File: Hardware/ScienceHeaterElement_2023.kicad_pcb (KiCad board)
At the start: 2 copper layers, 127 x 127.1 mm, 10 parts, among them Q1 BUK7M6R3-40EX, U1 LMT85DCK

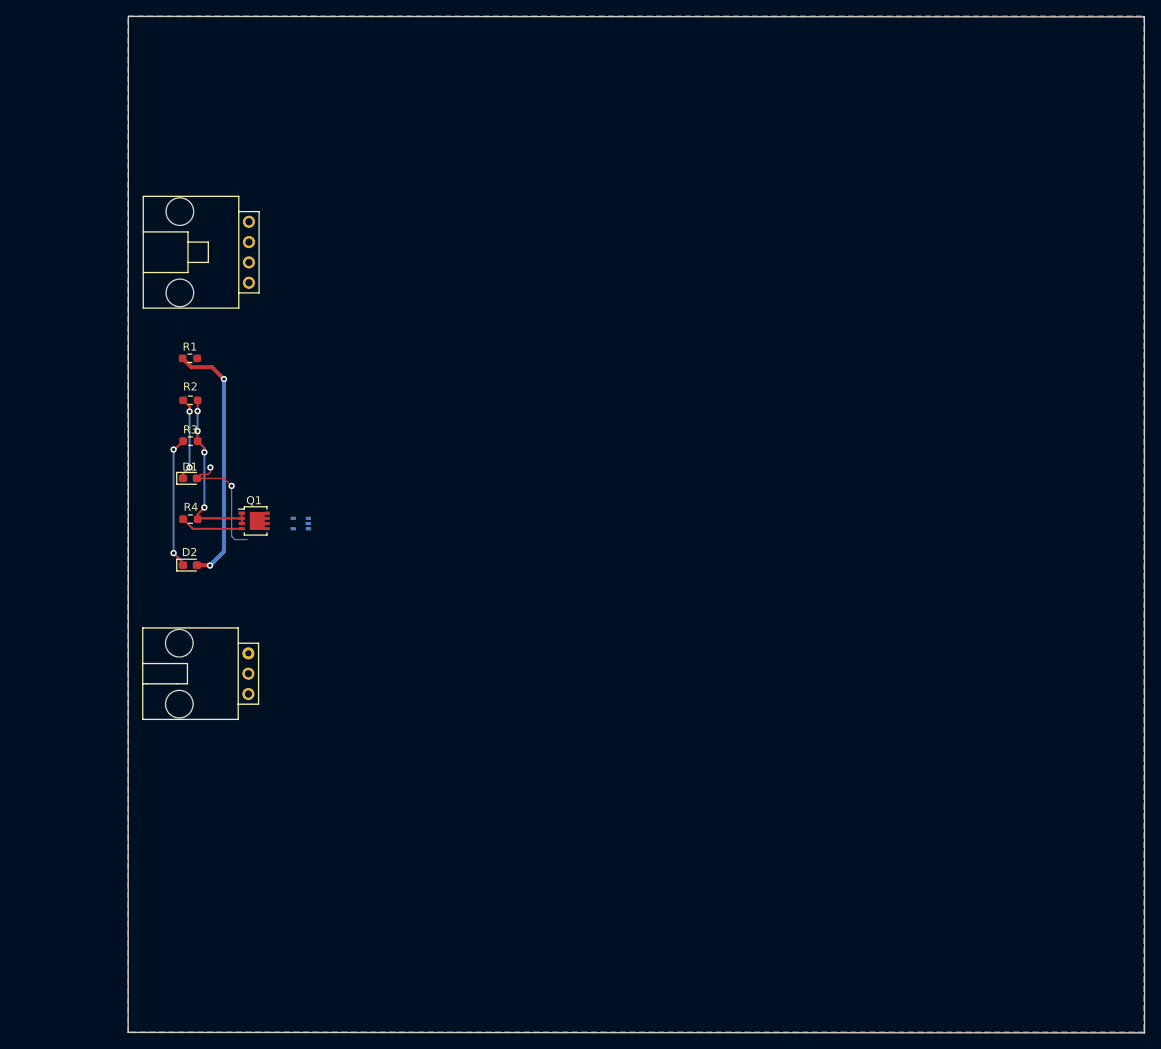
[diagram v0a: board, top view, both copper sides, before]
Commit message: Schematic Rework
Moved all devices to the back side of the board. Compressed the board down to a smaller area. Added heat traces and created a keep out area.
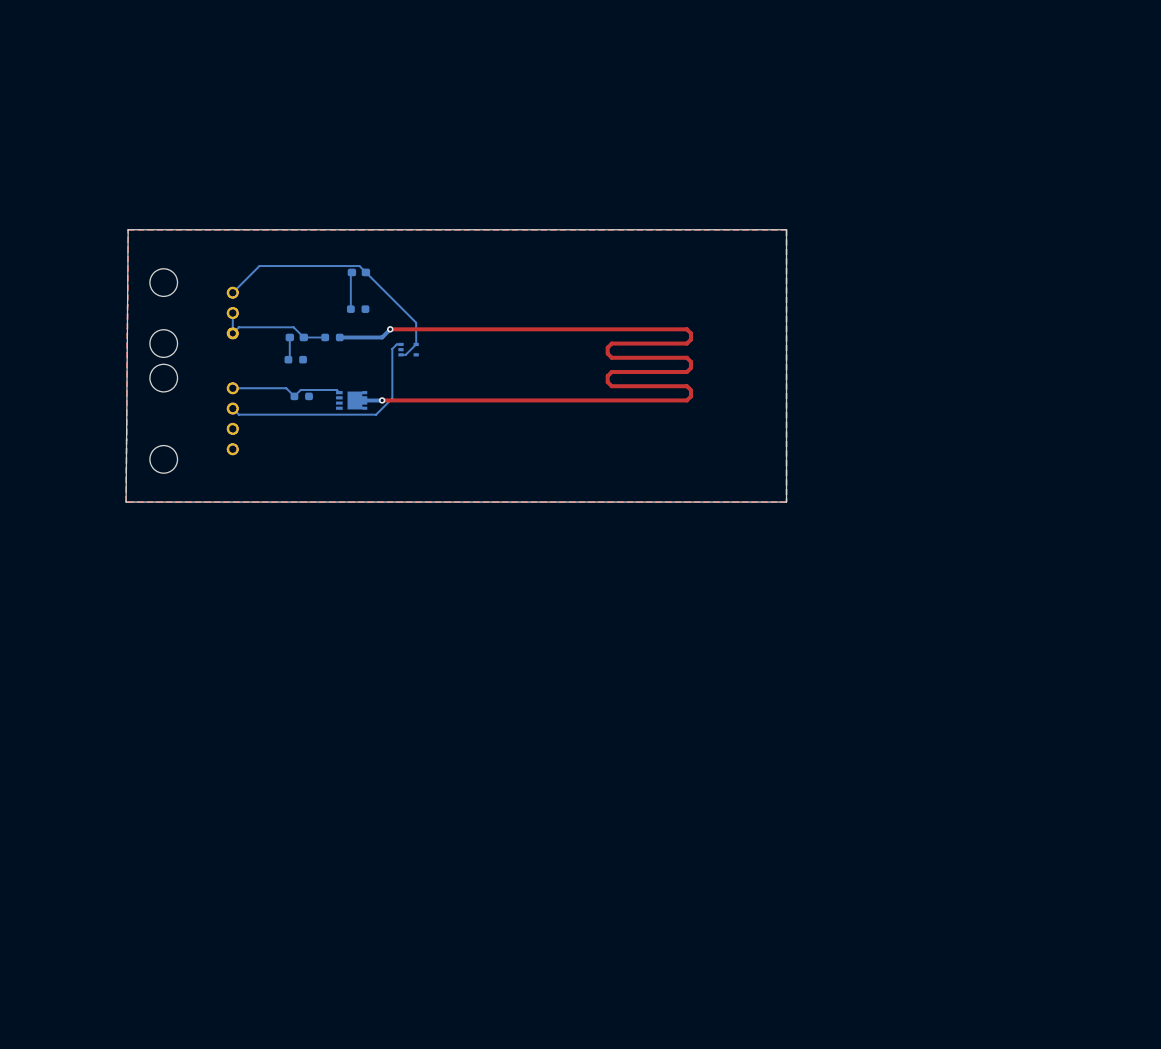
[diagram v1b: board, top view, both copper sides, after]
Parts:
- Conn1, Conn2, D1, D2, Q1, R1, R2, R3, R4: moved to B.Cu
- moved Conn1 50.2 mm to (84.2, 44.7), turned to -90 degrees
- moved D1 33.3 mm to (100.0, 42.2)
- moved D2 31.4 mm to (92.2, 50.3)
- moved U1 25.6 mm to (106.2, 51.8), turned to 0 degrees
- moved R2 23.9 mm to (99.9, 46.8)
- moved R4 20.7 mm to (92.8, 57.7)
- moved Q1 19.4 mm to (99.1, 58.2)
- moved R1 18.0 mm to (96.7, 50.3)
- moved R3 16.6 mm to (92.1, 53.1)
- moved Conn2 13.3 mm to (84.2, 56.6), turned to -90 degrees
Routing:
- net /Heater_Trace: track 0.13 -> 134.0 mm, vias 0 -> 2
- net Temp_Sense: track 0.00 -> 28.6 mm
- net GND: track 22.4 -> 0.02 mm, vias 4 -> 0
- net +12V: track 31.9 -> 14.9 mm, vias 2 -> 0
- net +3.3V: track 15.7 -> 32.4 mm, vias 2 -> 0
- net Net-(D2-K): track 16.6 -> 3.18 mm, vias 2 -> 0
- net Gate_Driving_Pin: track 7.83 -> 14.2 mm
- net Net-(D1-K): track 10.4 -> 4.64 mm, vias 2 -> 0
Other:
- board size 127 x 127.1 mm -> 82.5 x 34 mm

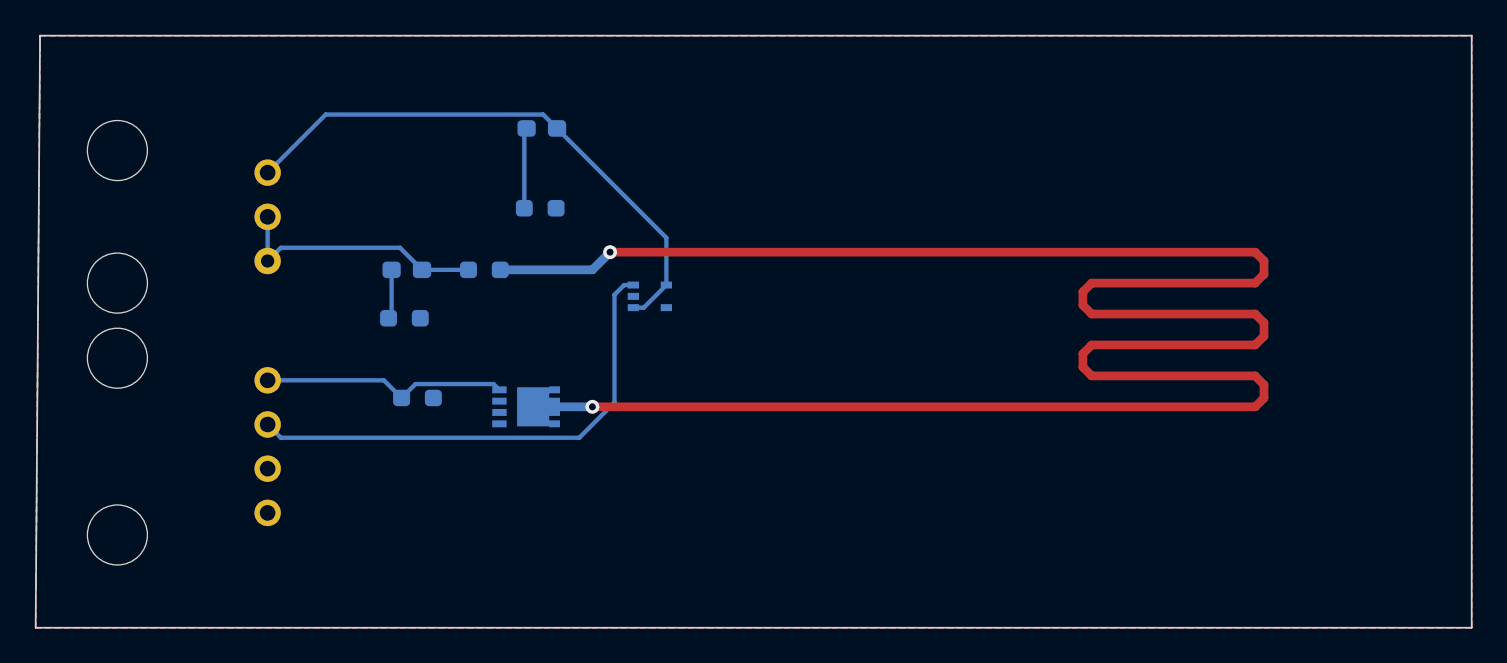
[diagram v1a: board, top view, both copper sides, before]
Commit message: Fixed edge cuts and ground plane
Fixed edge cuts to rounded edges and created one ground plane and then filled the area.
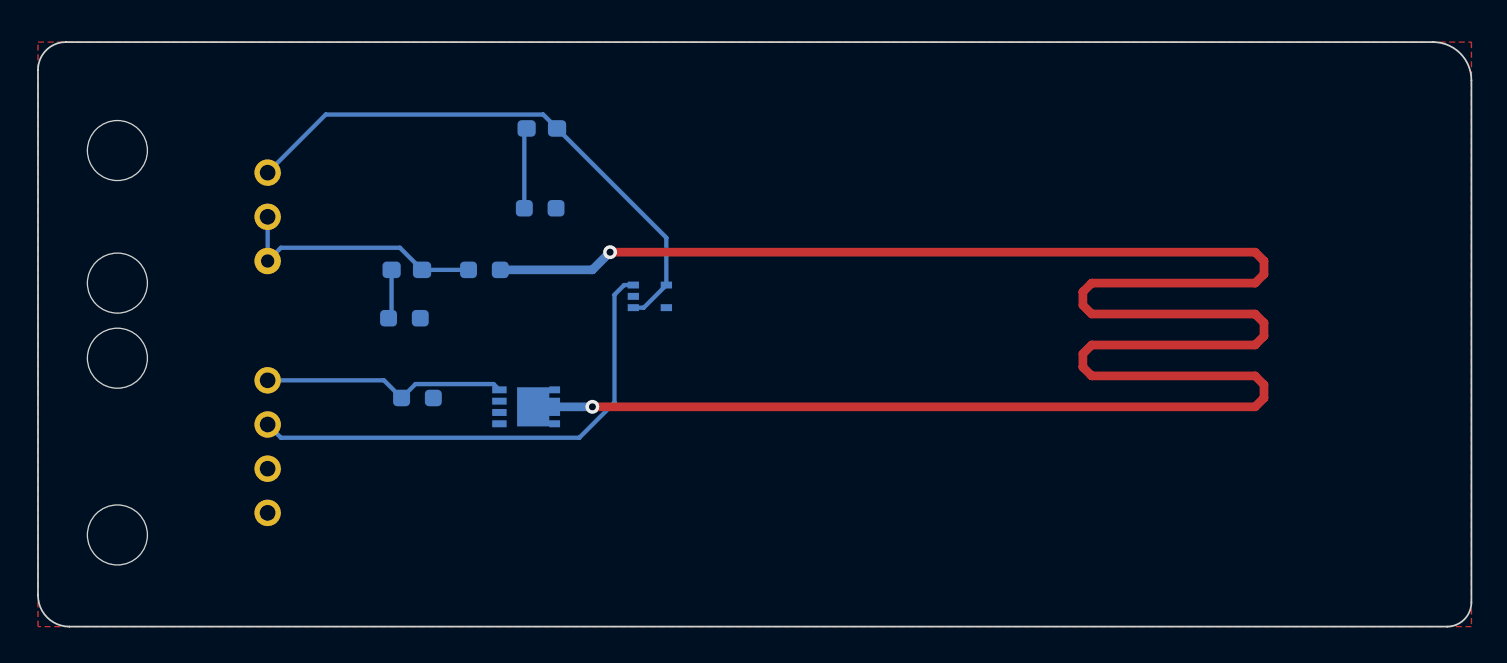
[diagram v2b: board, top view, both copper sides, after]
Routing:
- removed copper zone on B.Cu, net GND
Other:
- board size 82.5 x 34 mm -> 82.4 x 33.6 mm
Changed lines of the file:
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@@
     )
   )
-  (gr_line (start 153.416 36.83) (end 153.416 70.866)
+  (gr_line (start 153.4 39.4) (end 153.4 69.4)
     (stroke (width 0.1) (type default)) (layer "Edge.Cuts"))
-  (gr_line (start 153.416 70.866) (end 70.866 70.866)
+  (gr_line (start 71 38.8) (end 71 69)
     (stroke (width 0.1) (type default)) (layer "Edge.Cuts"))
-  (gr_line (start 70.866 70.866) (end 71.12 36.83)
+  (gr_arc (start 151.2 37.2) (mid 152.755635 37.844365) (end 153.4 39.4)
     (stroke (width 0.1) (type default)) (layer "Edge.Cuts"))
-  (gr_line (start 71.12 36.83) (end 153.416 36.83)
+  (gr_arc (start 72.8 70.8) (mid 71.527208 70.272792) (end 71 69)
+    (stroke (width 0.1) (type default)) (layer "Edge.Cuts"))
+  (gr_line (start 72.8 70.8) (end 152 70.8)
+    (stroke (width 0.1) (type default)) (layer "Edge.Cuts"))
+  (gr_arc (start 71 38.8) (mid 71.468629 37.668629) (end 72.6 37.2)
+    (stroke (width 0.1) (type default)) (layer "Edge.Cuts"))
+  (gr_line (start 151.2 37.2) (end 72.6 37.2)
+    (stroke (width 0.1) (type default)) (layer "Edge.Cuts"))
+  (gr_arc (start 153.4 69.4) (mid 152.989949 70.389949) (end 152 70.8)
     (stroke (width 0.1) (type default)) (layer "Edge.Cuts"))
   (segment (start 84.201 44.704) (end 87.541 41.364) (width 0.25) (layer "B.Cu") (net 1))
@@
   (segment (start 104.14 51.723) (end 104.14 57.921305) (width 0.25) (layer "B.Cu") (net 8))
   (segment (start 84.963 59.944) (end 102.117305 59.944) (width 0.25) (layer "B.Cu") (net 8))
-  (zone (net 2) (net_name "GND") (layers "F&B.Cu") (hatch edge 0.5)
+  (zone (net 2) (net_name "GND") (layer "F.Cu") (hatch edge 0.5)
     (priority 1)
     (connect_pads yes (clearance 0.5))
     (min_thickness 0.25) (filled_areas_thickness no)
-    (fill (thermal_gap 0.5) (thermal_bridge_width 0.5))
+    (fill yes (thermal_gap 0.5) (thermal_bridge_width 0.5))
     (polygon
       (pts
-        (xy 71.12 36.83)
-        (xy 153.416 36.83)
-        (xy 153.416 70.866)
-        (xy 70.866 70.866)
+        (xy 71 37.2)
+        (xy 153.4 37.2)
+        (xy 153.4 70.8)
+        (xy 71 70.8)
       )
     )
   )
-  (zone (net 2) (net_name "GND") (layers "F&B.Cu") (hatch edge 0.5)
-    (connect_pads yes (clearance 0.5))
-    (min_thickness 0.25) (filled_areas_thickness no)
-    (fill (thermal_gap 0.5) (thermal_bridge_width 0.5))
-    (polygon
-      (pts
-        (xy 70.866 70.866)
-        (xy 71.12 36.83)
-        (xy 153.416 36.83)
-        (xy 153.416 70.866)
-      )
-    )
-  )
-  (zone (net 0) (net_name "") (layers "F&B.Cu" "Edge.Cuts") (name "Heater") (hatch edge 0.5)
+  (zone (net 0) (net_name "") (layers "F.Cu" "Edge.Cuts") (name "Heater") (hatch edge 0.5)
     (connect_pads (clearance 0))
     (min_thickness 0.25) (filled_areas_thickness no)

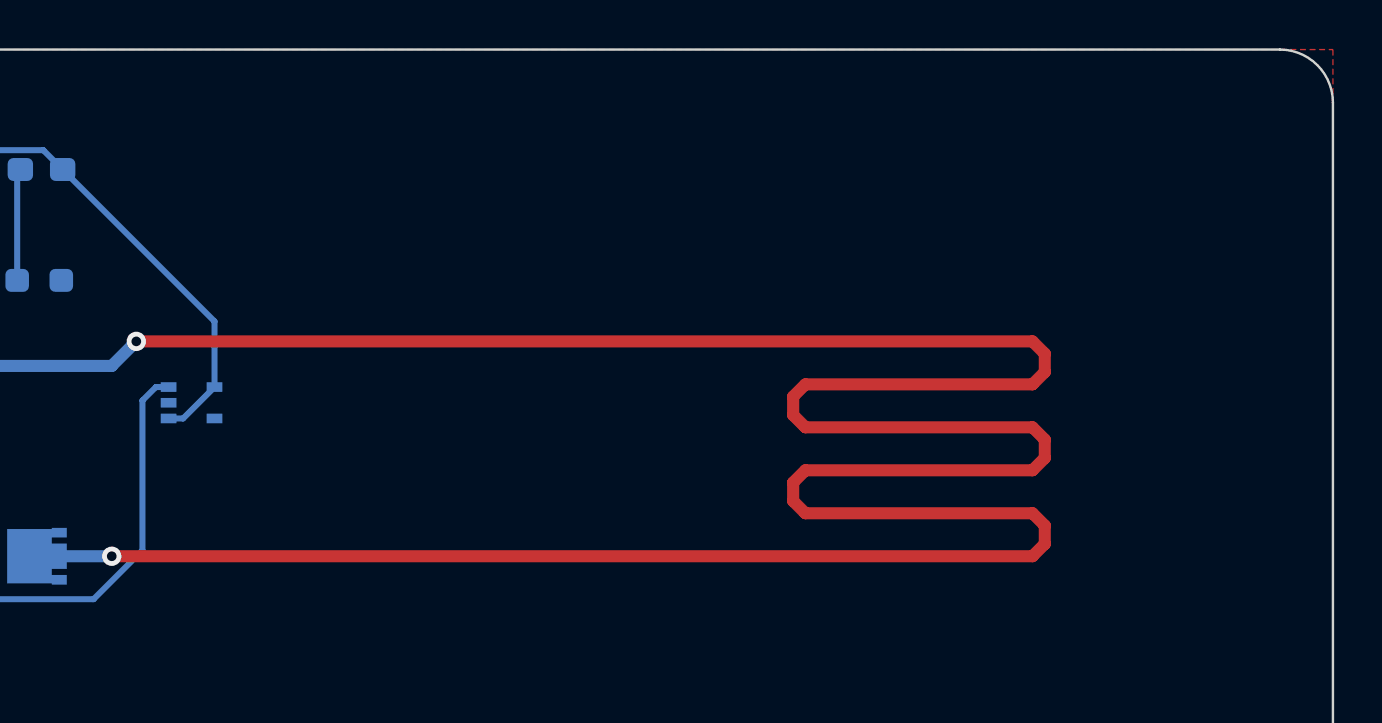
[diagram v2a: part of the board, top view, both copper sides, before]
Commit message: Updated Silkscreen
Updated silkscreen with warning symbols
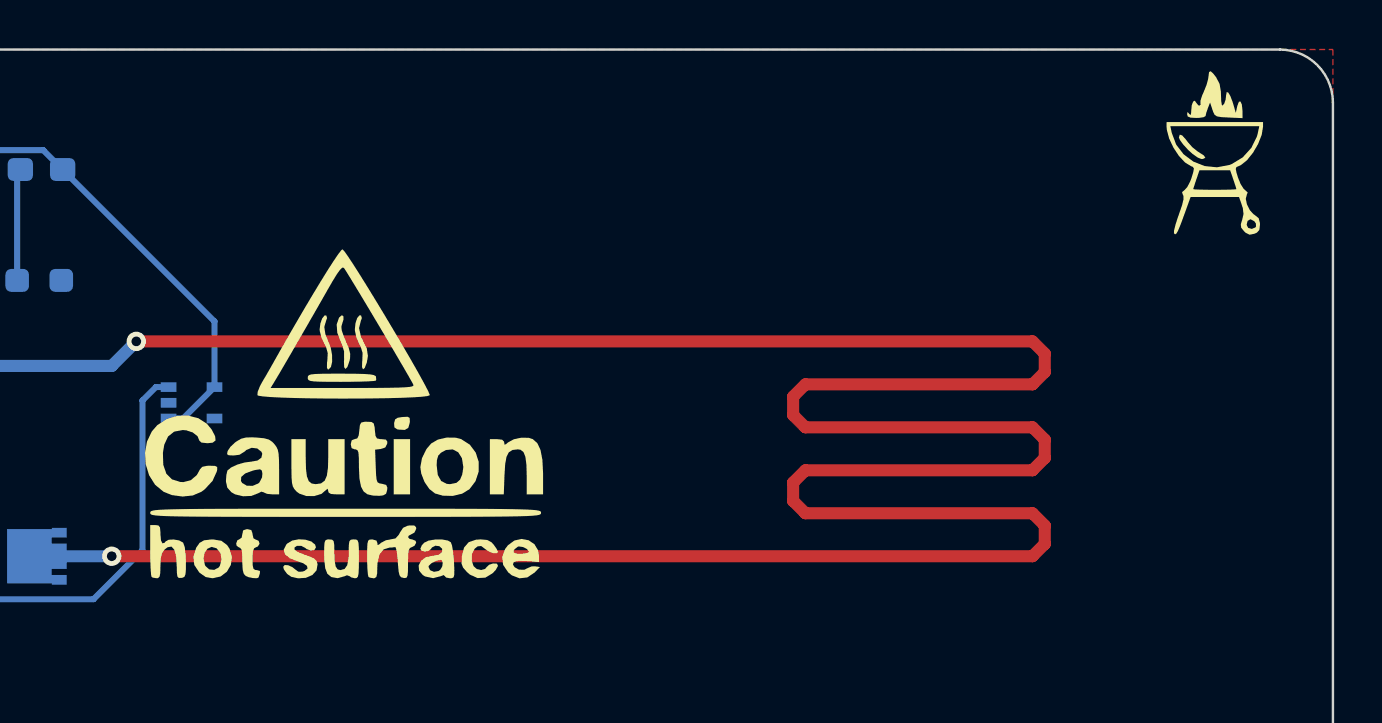
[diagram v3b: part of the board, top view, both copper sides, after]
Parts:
- added G***: LOGO, LOGO, F.Cu at (148.5, 41.2)
- added G***: LOGO, LOGO, F.Cu at (112.4, 52.2)
